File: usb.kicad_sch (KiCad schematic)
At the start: 129 parts, among them J3 USB4105-GF-A, J4 WE_632723300011_alt_symbol, Q1 PJE138K, Q2 PJE138K, Q3 PJE138K, U10 TUSB1046-DCI, U11 TPD4E05U06QDQARQ1, U12 AP22615, U13 TPD4E05U06QDQARQ1, U14 TPD4E05U06QDQARQ1, U15 TPD4E05U06QDQARQ1, U16 TPD4E05U06QDQARQ1, U5 FT230XQ-R, U6 TPS65988, U7 W25Q80DVUXIE_TR, U8 NCP730BMT330TBG, U9 AP22615

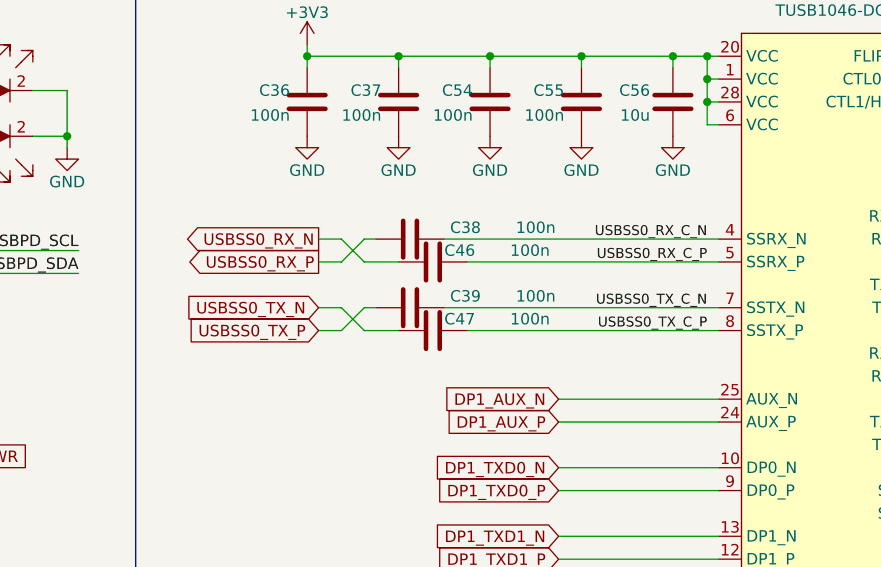
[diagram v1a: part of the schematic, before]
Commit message: Replace USB SS SOM-MUX capacitors with ORs
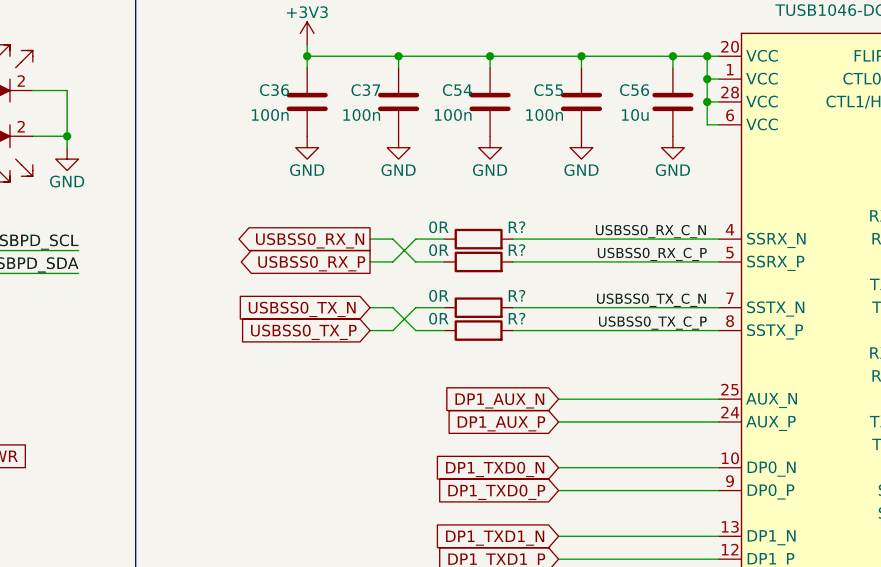
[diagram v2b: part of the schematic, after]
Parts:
- removed C38, C39, C46, C47: C_100n_0402, jetson-orin-baseboard-footprints:0402-cap, symbol jetson-orin-baseboard:C_100n_0402
- added R? (x4): R_0R_0402, jetson-orin-baseboard-footprints:0402-res, symbol jetson-orin-baseboard:R_0R_0402
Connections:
- net USBSS0_RX_C_N: now also R?.2
- net USBSS0_RX_C_P: now also R?.2
- net USBSS0_RX_N: now also R?.1
- net USBSS0_RX_P: now also R?.1
- net USBSS0_TX_C_N: now also R?.2
- net USBSS0_TX_C_P: now also R?.2
- net USBSS0_TX_N: now also R?.1
- net USBSS0_TX_P: now also R?.1

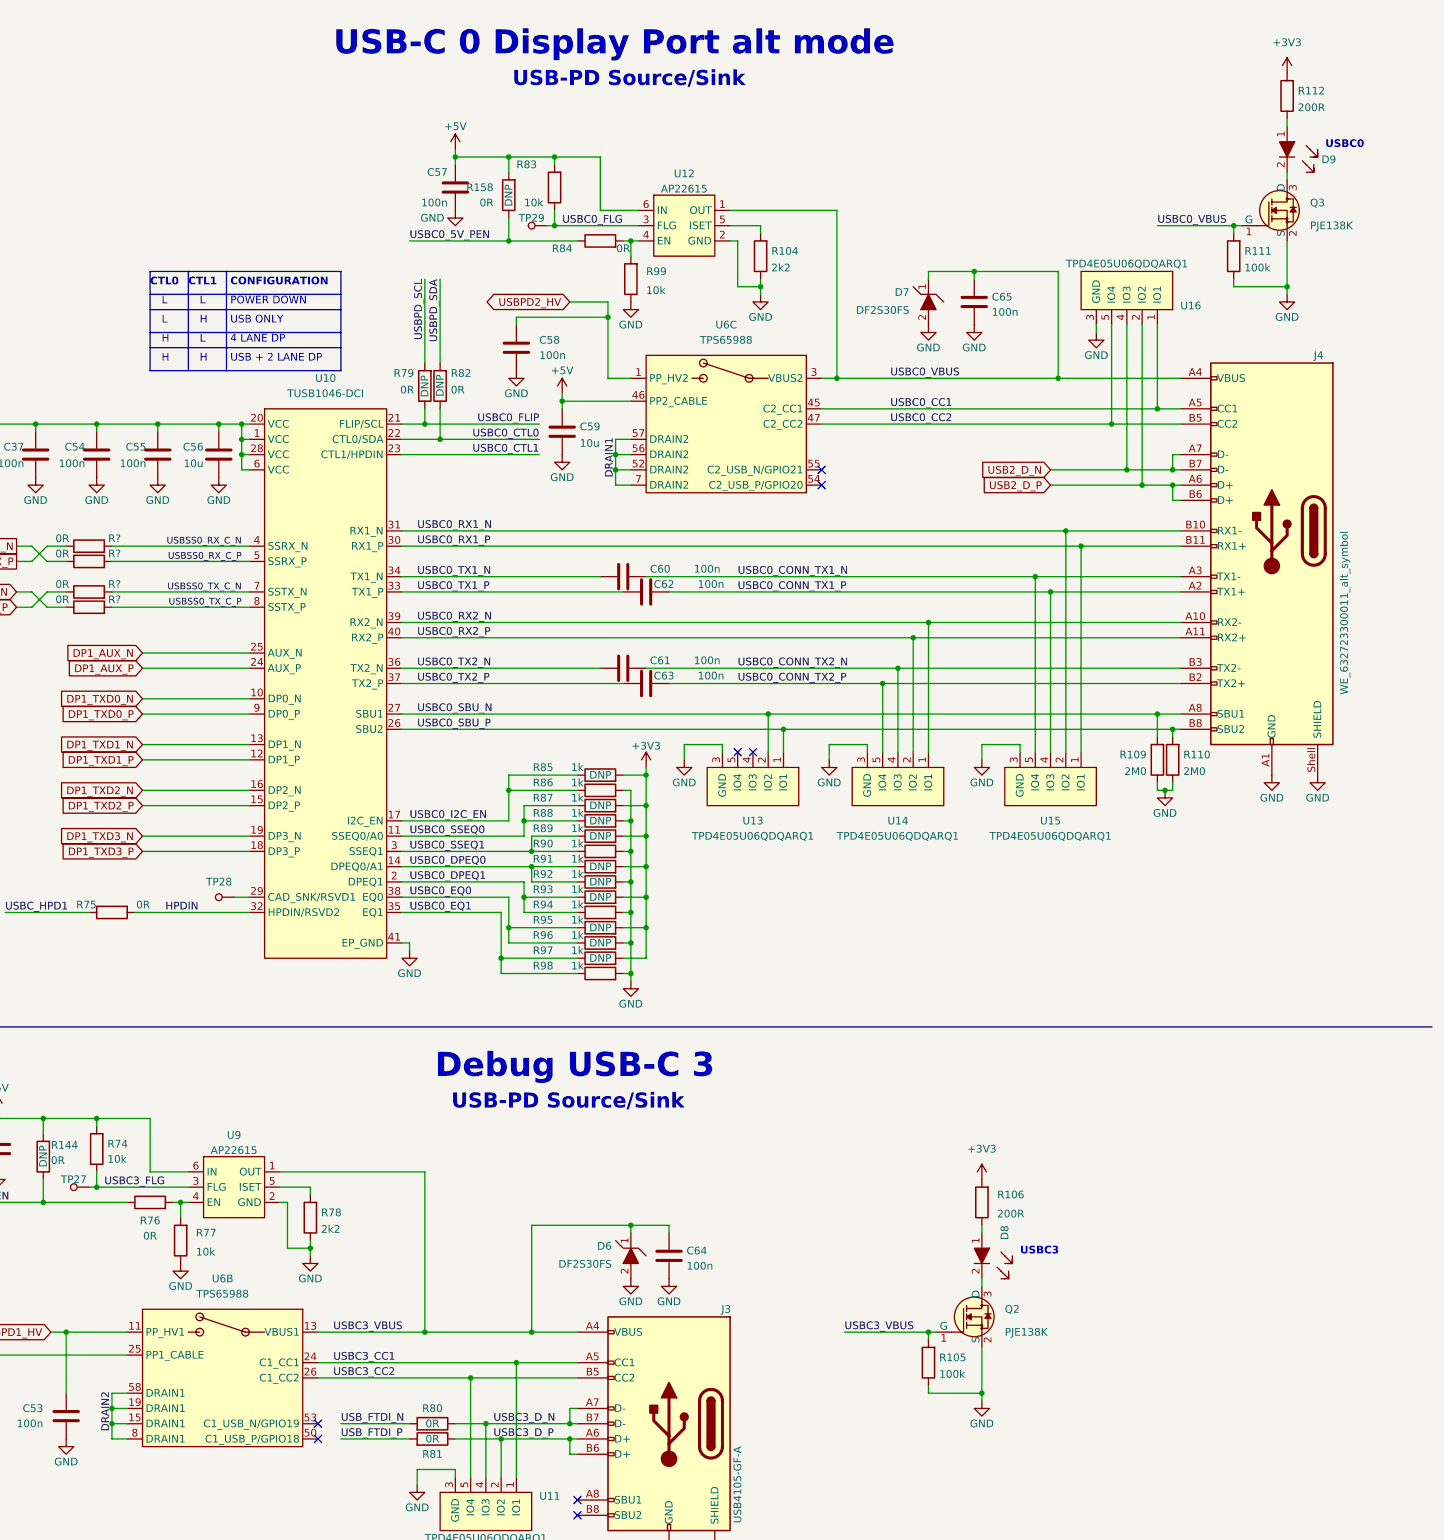
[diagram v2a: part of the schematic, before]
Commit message: Power USB VBUS leds directly from VBUS
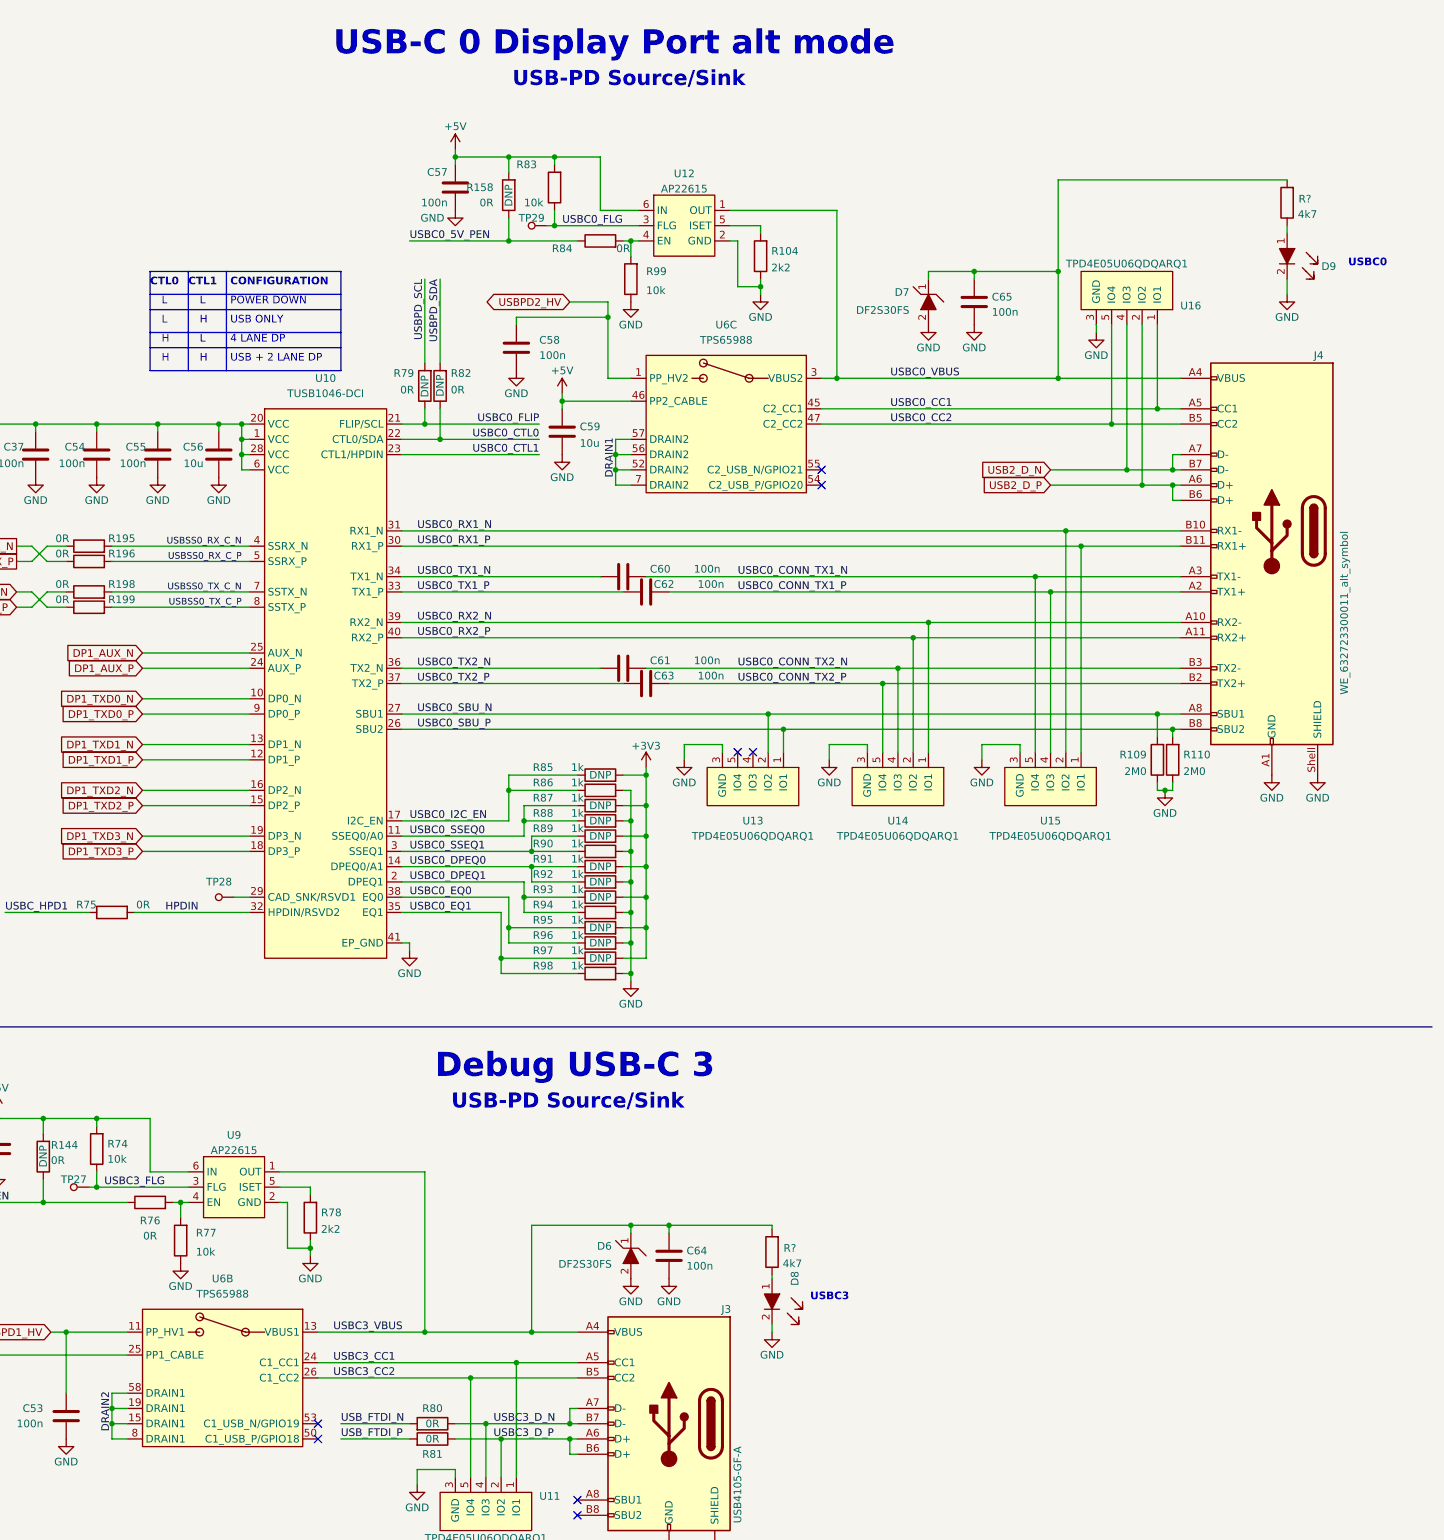
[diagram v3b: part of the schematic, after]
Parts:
- removed Q2, Q3: PJE138K, antmicro-footprints:SOT-523, symbol antmicroTransistorsFETsMOSFETsSingle:PJE138K
- removed R105, R111: R_100k_0402, jetson-orin-baseboard-footprints:0402-res, symbol jetson-orin-baseboard:R_100k_0402
- removed R106, R112: R_200R_0402, jetson-orin-baseboard-footprints:0402-res, symbol jetson-orin-baseboard:R_200R_0402
- added R? (x2): R_4k7_0402, jetson-orin-baseboard-footprints:0402-res, symbol jetson-orin-baseboard:R_4k7_0402
- gave numbers to parts that had none: 4
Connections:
- net GND: now also D8.2, D9.2
- net USBC0_VBUS: now also R?.2
- net USBC3_VBUS: now also R?.2
- net at D8.1: now also R?.1
- net at D9.1: now also R?.1
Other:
- moved on the sheet: D8, D9

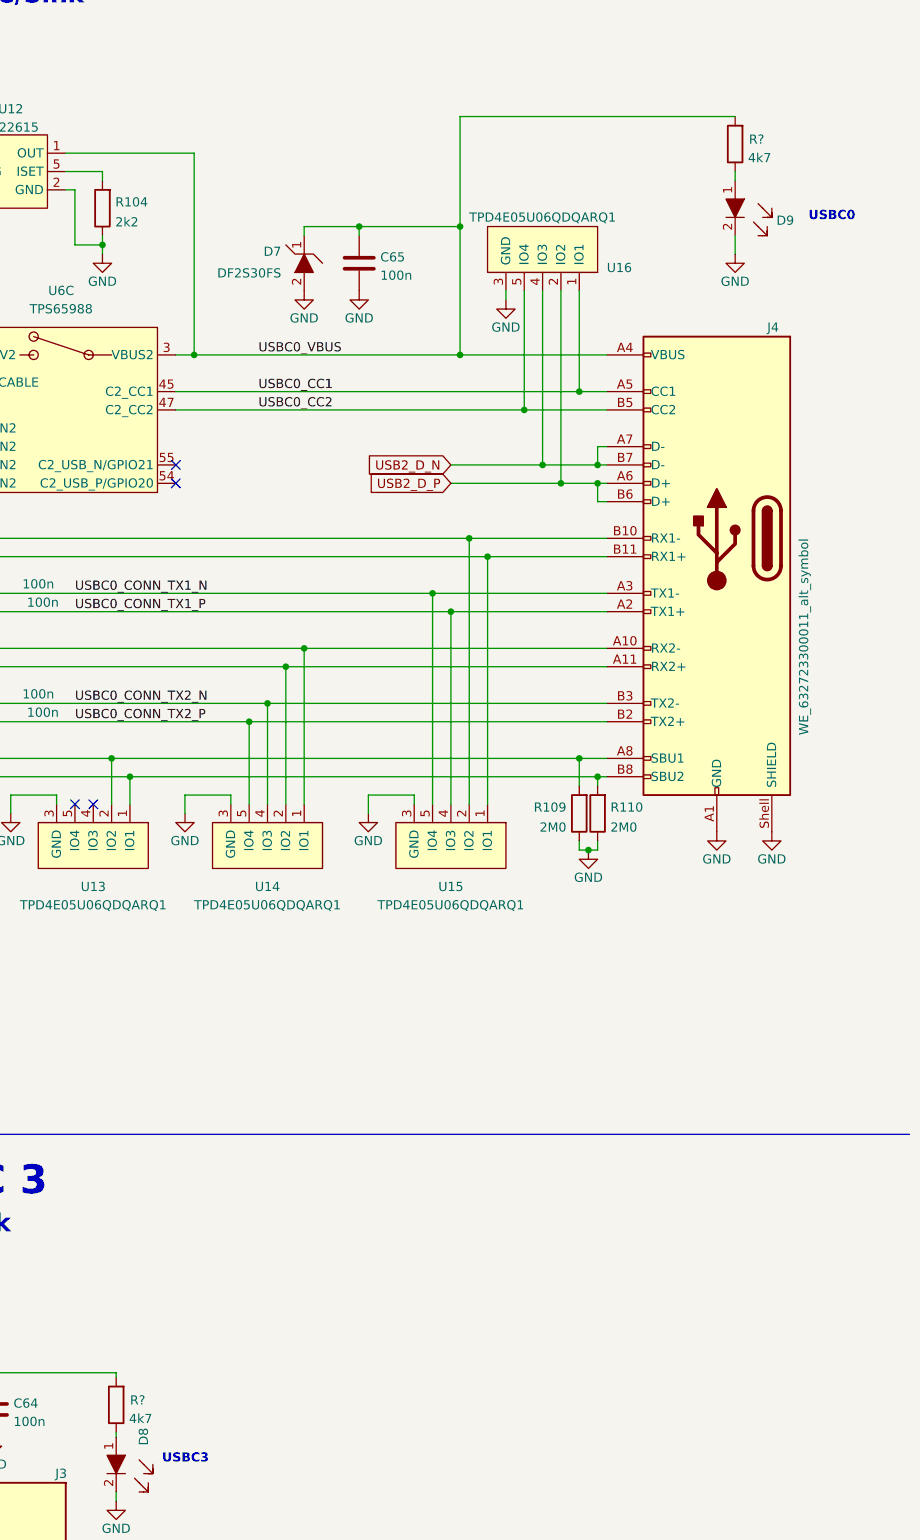
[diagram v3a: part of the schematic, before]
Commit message: Continue routing after changes
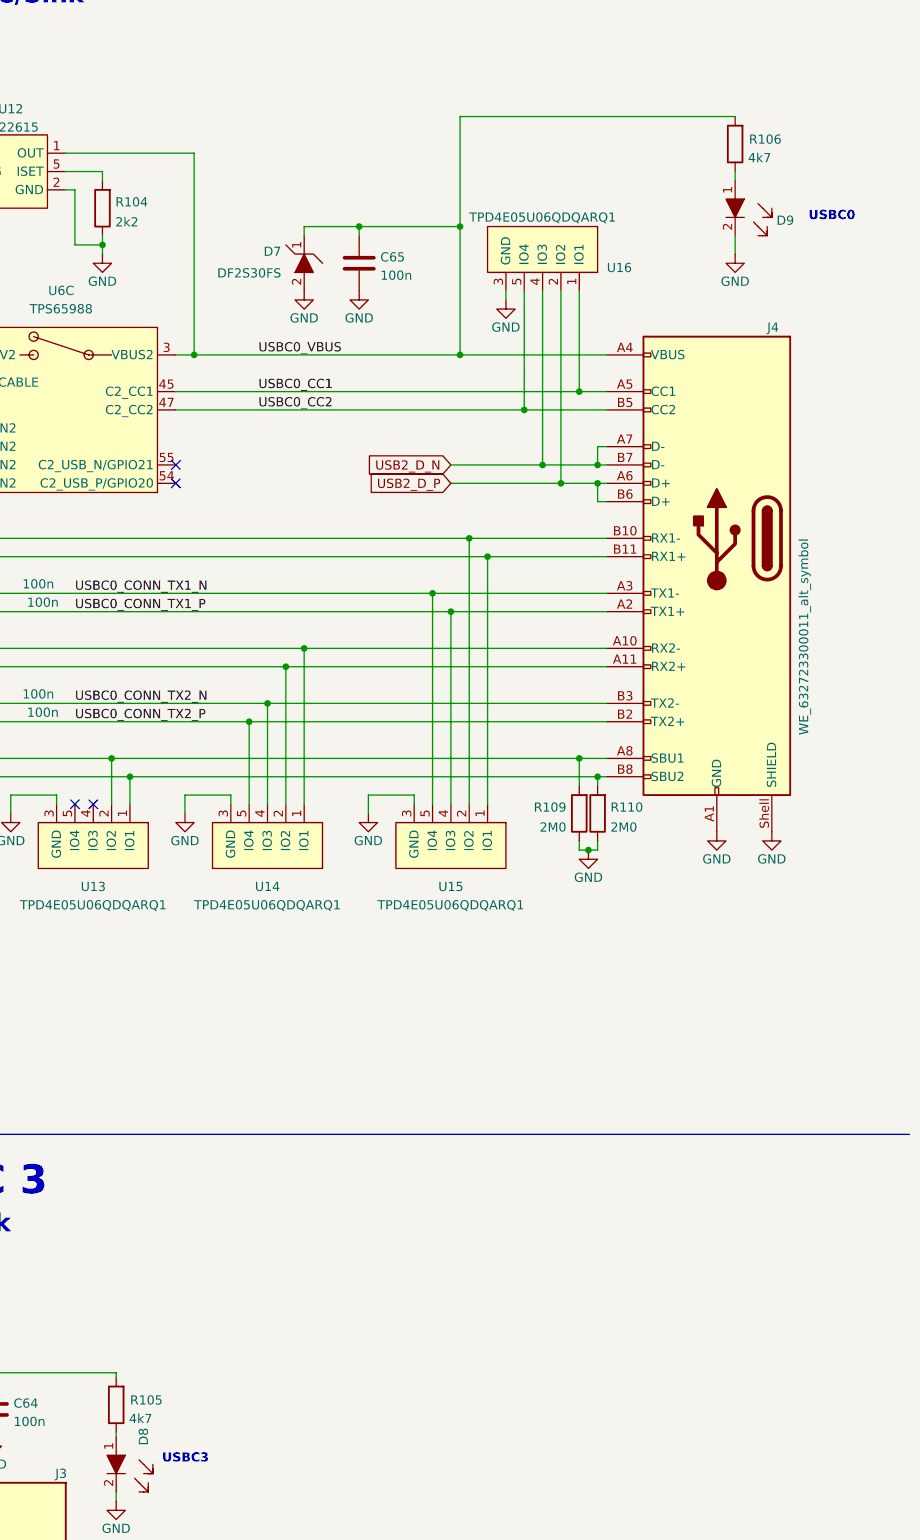
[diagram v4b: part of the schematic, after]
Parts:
- gave numbers to parts that had none: 2
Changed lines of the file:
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@@
   (symbol (lib_id "jetson-orin-baseboard:R_4k7_0402") (at 383.54 44.45 90) (unit 1)
     (in_bom yes) (on_board yes)
-    (property "Reference" "R?" (id 0) (at 385.445 43.815 90)
+    (property "Reference" "R106" (id 0) (at 385.445 43.815 90)
       (effects (font (size 1.27 1.27)) (justify right))
     )
@@
   (symbol (lib_id "jetson-orin-baseboard:R_4k7_0402") (at 297.815 219.075 90) (unit 1)
     (in_bom yes) (on_board yes)
-    (property "Reference" "R?" (id 0) (at 299.72 218.44 90)
-      (effects (font (size 1.27 1.27)) (justify right))
-    )
+    (property "Reference" "R105" (id 0) (at 299.72 218.44 90)
+      (effects (font (size 1.27 1.27)) (justify right))
+    )
